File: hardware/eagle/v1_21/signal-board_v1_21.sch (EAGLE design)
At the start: 7 parts

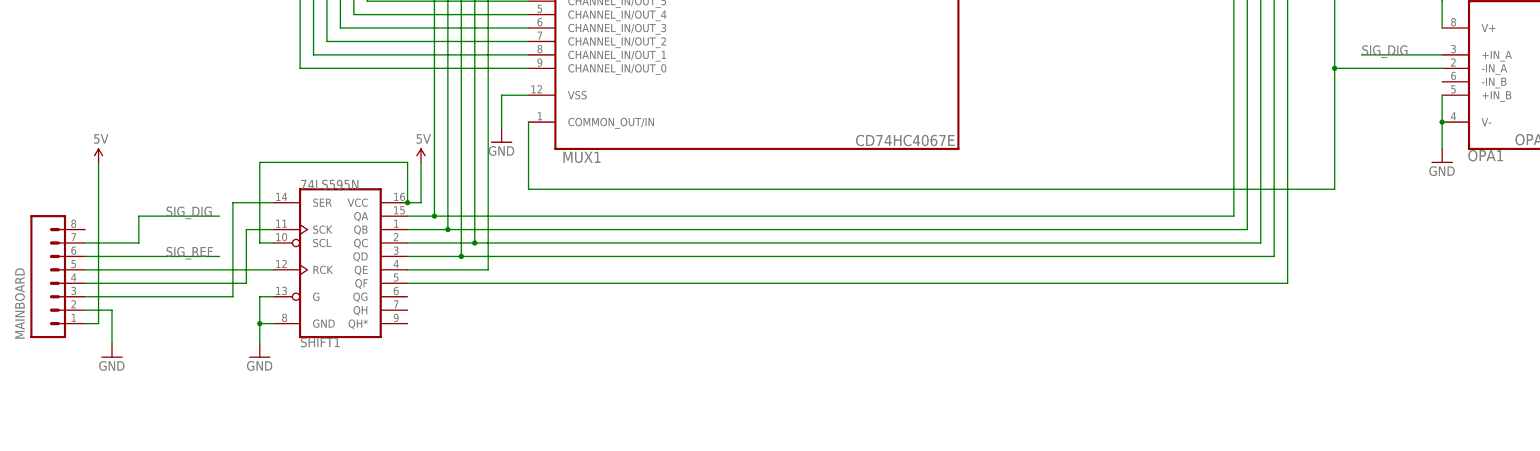
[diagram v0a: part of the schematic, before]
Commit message: Corrected an error in the signal board schematic. GND was connected to OPA1's +IN_B.
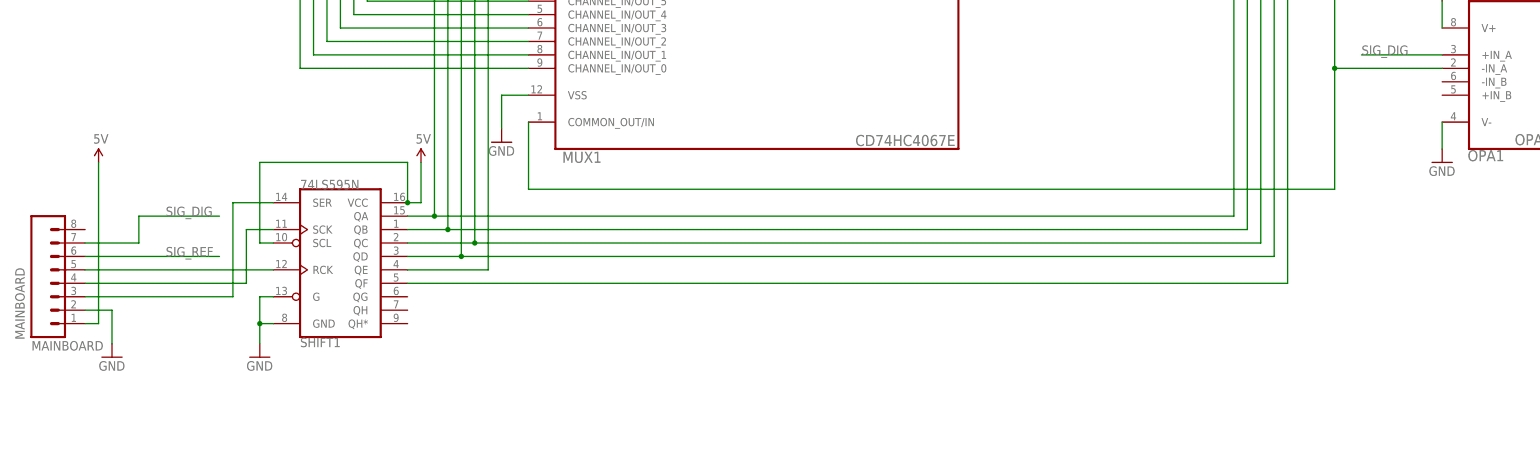
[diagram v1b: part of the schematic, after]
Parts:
- MAINBOARD: value (none) -> MAINBOARD
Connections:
- net GND: no longer OPA1.+IN_B
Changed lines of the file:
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@@
 <?xml version="1.0" encoding="utf-8"?>
 <!DOCTYPE eagle SYSTEM "eagle.dtd">
-<eagle version="7.5.0">
+<eagle version="7.6.0">
 <drawing>
 <settings>
@@
 <part name="U$3" library="SparkFun-Aesthetics" deviceset="5V" device=""/>
 <part name="GND3" library="SparkFun-Aesthetics" deviceset="GND" device=""/>
-<part name="MAINBOARD" library="SparkFun-Connectors" deviceset="M08" device="LONGPADS"/>
+<part name="MAINBOARD" library="SparkFun-Connectors" deviceset="M08" device="LONGPADS" value="MAINBOARD"/>
 <part name="U$4" library="SparkFun-Aesthetics" deviceset="5V" device=""/>
 <part name="GND4" library="SparkFun-Aesthetics" deviceset="GND" device=""/>
 <part name="U$5" library="SparkFun-Aesthetics" deviceset="5V" device=""/>
 <part name="GND5" library="SparkFun-Aesthetics" deviceset="GND" device=""/>
-<part name="FRAME1" library="frames" deviceset="A3L-LOC" device=""/>
+<part name="FRAME1" library="frames" deviceset="A3L-LOC" device="" value="FRAME"/>
 </parts>
 <sheets>
@@
 <segment>
 <pinref part="OPA1" gate="A" pin="V-"/>
-<wire x1="144.78" y1="114.3" x2="144.78" y2="109.22" width="0.1524" layer="91"/>
 <pinref part="GND5" gate="1" pin="GND"/>
-<pinref part="OPA1" gate="A" pin="+IN_B"/>
-<junction x="144.78" y="109.22"/>
 <wire x1="144.78" y1="109.22" x2="144.78" y2="104.14" width="0.1524" layer="91"/>
 </segment>
